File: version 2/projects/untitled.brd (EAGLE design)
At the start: 32.2 x 80.5 mm, 27 parts, among them IC1 LM1117IMPX-3.3, U1 FT232RLSSOP, U2 MCP73831, X2 USB-SMD-NS

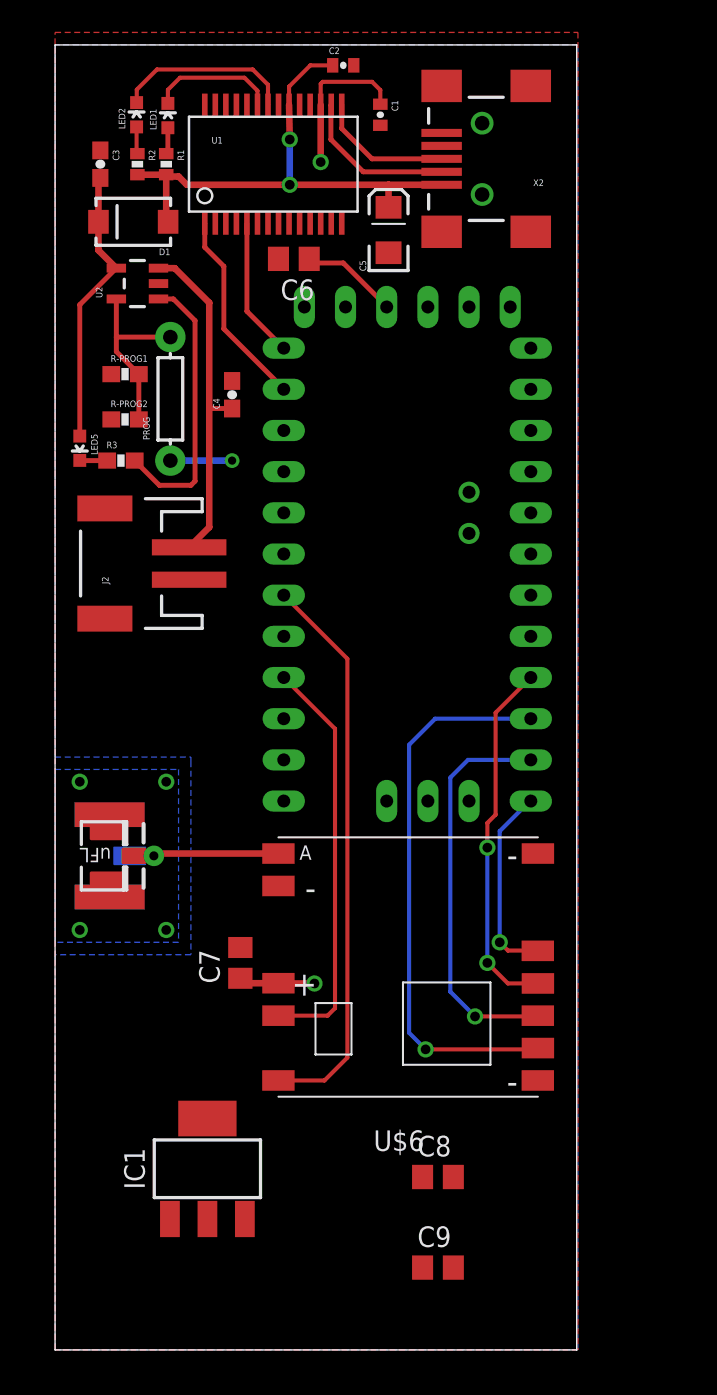
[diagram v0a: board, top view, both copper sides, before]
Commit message: connected \!DTR Pin to RST
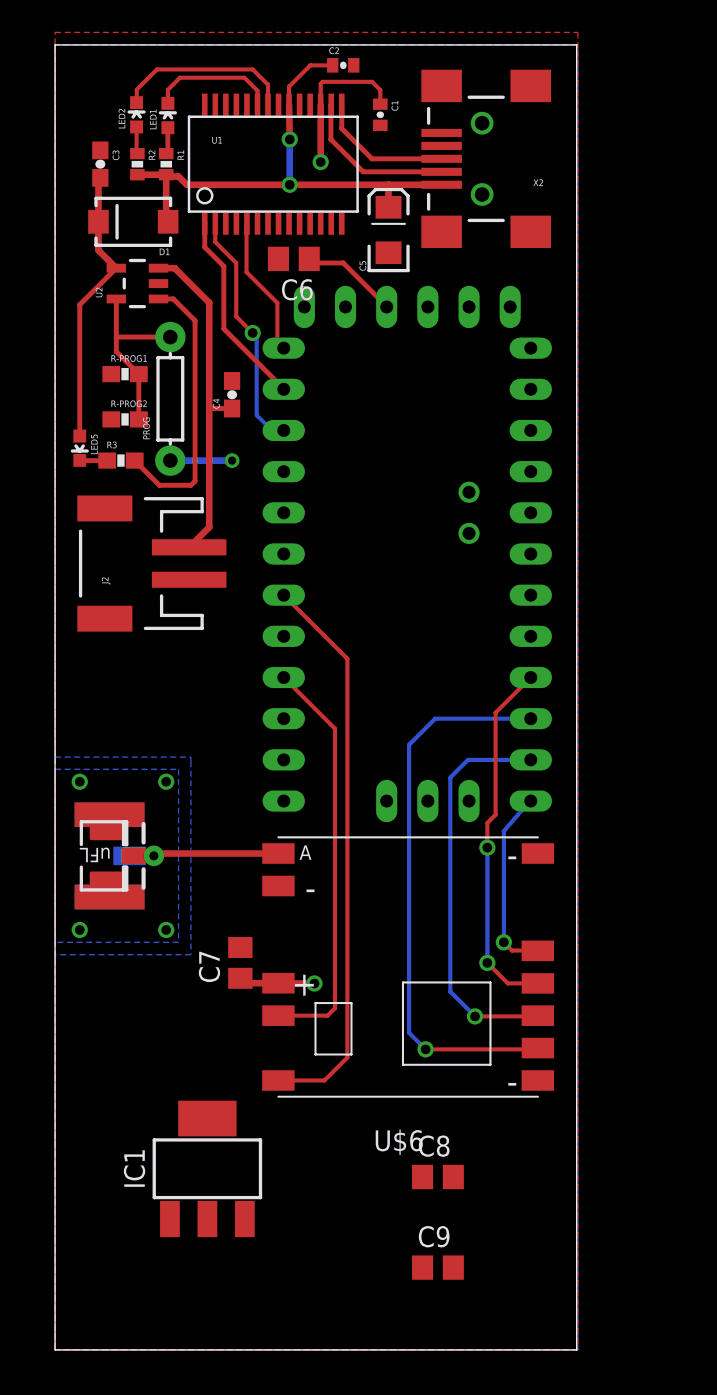
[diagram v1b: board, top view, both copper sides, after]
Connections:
- removed net N$7: U$1.RST1
- net DTR: now also U$1.RST1
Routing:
- net DTR: track 0.00 -> 14.9 mm, vias 0 -> 1
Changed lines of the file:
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@@
 <contactref element="IC1" pad="1"/>
 <wire x1="4.1275" y1="28.448" x2="4.0005" y2="29.51775" width="0" layer="19" extent="1-1"/>
+<wire x1="14.544" y1="67.818" x2="13.899" y2="70.004" width="0" layer="19" extent="1-1"/>
 <wire x1="16.499" y1="77.316" x2="19.192" y2="79.756" width="0" layer="19" extent="1-1"/>
 <wire x1="14.549" y1="77.316" x2="16.499" y2="77.316" width="0" layer="19" extent="1-1"/>
-</signal>
-<signal name="N$7">
-<contactref element="U$1" pad="RST1"/>
 </signal>
 <signal name="N$9">
@@
 <signal name="DTR">
 <contactref element="U1" pad="2"/>
+<contactref element="U$1" pad="RST1"/>
+<wire x1="10.649" y1="68.853" x2="10.649" y2="70.004" width="0.254" layer="1"/>
+<wire x1="11.938" y1="64.262" x2="12.954" y2="63.246" width="0.254" layer="1"/>
+<via x="12.954" y="63.246" extent="1-16" drill="0.6"/>
+<wire x1="11.938" y1="67.564" x2="10.649" y2="68.853" width="0.254" layer="1"/>
+<wire x1="11.938" y1="67.564" x2="11.938" y2="64.262" width="0.254" layer="1"/>
+<wire x1="12.954" y1="63.246" x2="13.208" y2="62.992" width="0.254" layer="16"/>
+<wire x1="13.208" y1="62.992" x2="13.208" y2="58.166" width="0.254" layer="16"/>
+<wire x1="13.208" y1="58.166" x2="14.14409375" y2="57.22990625" width="0.254" layer="16"/>
+<wire x1="14.14409375" y1="57.22990625" x2="14.8714625" y2="57.22990625" width="0.254" layer="16"/>
 </signal>
 <signal name="3.3V" class="1">
@@
 <contactref element="U1" pad="5"/>
 <contactref element="U$1" pad="TX0"/>
-<wire x1="12.599" y1="70.004" x2="12.599" y2="64.58236875" width="0.3048" layer="1"/>
-<wire x1="12.599" y1="64.58236875" x2="14.8714625" y2="62.30990625" width="0.3048" layer="1"/>
+<wire x1="14.8714625" y1="62.30990625" x2="14.478" y2="62.30990625" width="0.254" layer="1"/>
+<wire x1="14.478" y1="65.096628125" x2="12.574171875" y2="67.00045625" width="0.254" layer="1"/>
+<wire x1="12.574171875" y1="67.00045625" x2="12.574171875" y2="69.979171875" width="0.254" layer="1"/>
+<wire x1="12.574171875" y1="69.979171875" x2="12.599" y2="70.004" width="0.254" layer="1"/>
+<wire x1="14.478" y1="62.30990625" x2="14.478" y2="65.096628125" width="0.254" layer="1"/>
 </signal>
 <signal name="POWER">
@@
 <contactref element="U$6" pad="NSS"/>
 <wire x1="30.1114625" y1="34.36990625" x2="30.05190625" y2="34.36990625" width="0.254" layer="1"/>
-<wire x1="28.194" y1="25.654" x2="28.702" y2="25.146" width="0.254" layer="1"/>
-<wire x1="28.702" y1="25.146" x2="30.5265" y2="25.146" width="0.254" layer="1"/>
-<wire x1="30.5265" y1="25.146" x2="30.5425" y2="25.13" width="0.254" layer="1"/>
+<wire x1="30.5425" y1="25.13" x2="30.5265" y2="25.146" width="0.254" layer="1"/>
 <wire x1="30.1114625" y1="34.36990625" x2="30.05190625" y2="34.36990625" width="0.254" layer="16"/>
-<wire x1="30.05190625" y1="34.36990625" x2="28.194" y2="32.512" width="0.254" layer="16"/>
-<wire x1="28.194" y1="32.512" x2="28.194" y2="25.654" width="0.254" layer="16"/>
-<via x="28.194" y="25.654" extent="1-16" drill="0.6"/>
+<wire x1="30.05190625" y1="34.36990625" x2="28.448" y2="32.512" width="0.254" layer="16"/>
+<wire x1="28.448" y1="32.512" x2="28.448" y2="25.654" width="0.254" layer="16"/>
+<via x="28.448" y="25.654" extent="1-16" drill="0.6"/>
+<wire x1="30.5265" y1="25.146" x2="28.956" y2="25.146" width="0.254" layer="1"/>
+<wire x1="28.956" y1="25.146" x2="28.448" y2="25.654" width="0.254" layer="1"/>
 </signal>
 <signal name="N$3">

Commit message: reworked layout. Added voltage controller and discharging mechanism
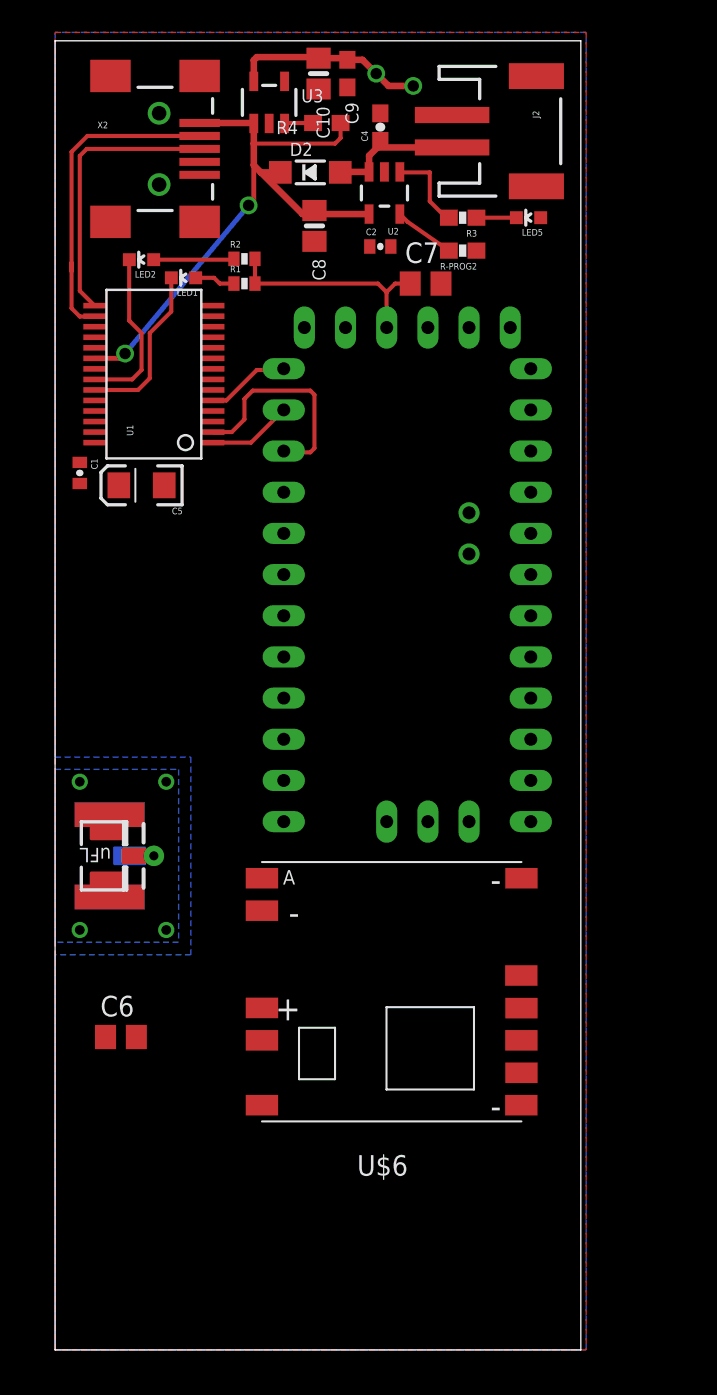
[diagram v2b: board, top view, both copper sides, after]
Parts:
- removed C3: 4.7uF, SparkFun-Capacitors:0603-CAP
- removed D1: MBRA140, SparkFun-DiscreteSemi:SMA-DIODE
- removed IC1: LM1117IMPX-3.3, lm1117:SOT223
- removed PROG: (no value), SparkFun-Resistors:AXIAL-0.3
- removed R-PROG1: 2k, SparkFun-Resistors:0603-RES
- added C10: 10µF, microbuilder:0805-NO
- added D2: MBR120, microbuilder:SOD-123
- added R4: 100k, microbuilder:0603-NO
- added U3: SPX3819-3.3, microbuilder:SOT23-5
- C4: value 4.7uF -> 10u
- C8: value 10u -> 10µF; device rcl:C0805 -> microbuilder:0805-NO
- C9: value 10u -> 1uF; device rcl:C0805 -> microbuilder:0603-NO
- moved C9 73.9 mm to (18.8, 79.2), turned to 270 degrees
- moved C8 59.2 mm to (16.8, 69.8), turned to 270 degrees
- moved C6 49.2 mm to (4.83, 19.8), turned to 0 degrees
- moved C7 43.4 mm to (23.6, 66.3), turned to 0 degrees
- moved J2 35.6 mm to (29.0, 75.7), turned to 270 degrees
- moved LED5 31.1 mm to (30.0, 70.4), turned to 90 degrees
- moved C1 28.8 mm to (2.29, 54.6)
- moved R3 25.9 mm to (25.9, 70.4), turned to 180 degrees
- moved R-PROG2 23.3 mm to (25.9, 68.3), turned to 180 degrees
- moved C5 21.9 mm to (6.10, 53.8), turned to 180 degrees
- moved X2 19.9 mm to (7.18, 74.6), turned to 0 degrees
- moved C4 18.9 mm to (20.8, 75.9)
- moved U2 16.2 mm to (21.1, 71.9), turned to 180 degrees
- moved U1 14.9 mm to (6.86, 60.7), turned to 90 degrees
- moved C2 11.4 mm to (20.8, 68.6)
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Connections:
- removed net N$3: C3.2, D1.C, LED5.A, U2.4
- removed net VCHARGE: C4.1, J2.2, U2.3
- new net +3V3: LED5.A
- new net 123: C1.1, U1.17
- new net EN: R4.2, U3.3
- new net VBAT: C4.1, D2.A, J2.2, U2.3
- net 3.3V: now also C10.1, R1.2, R2.2, U3.5; no longer C1.1, IC1.2, IC1.TAB, U1.17
- net 5V: now also D2.C, R4.1, U2.4, U3.1; no longer D1.A, IC1.3, R1.2, R2.2
- net GND: now also C10.2, U3.2; no longer C3.1, IC1.1, PROG.P$1, R-PROG1.1
- net LOL: no longer PROG.P$2, R-PROG1.2
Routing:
- net D4: track 35.0 -> 0.00 mm
- net MISO: track 34.5 -> 0.00 mm, vias 1 -> 0
- net D6: track 25.4 -> 0.00 mm
- net MOSI: track 24.7 -> 0.00 mm, vias 1 -> 0
- net SCL: track 22.4 -> 0.00 mm, vias 2 -> 0
- net VCHARGE: track 21.1 -> 0.00 mm
- net N$3: track 17.7 -> 0.00 mm
- net N$6: track 17.2 -> 5.24 mm
- net CS: track 11.7 -> 0.00 mm, vias 1 -> 0
- net USB_D-: track 9.81 -> 20.1 mm
- net USB_D+: track 8.39 -> 17.2 mm
- net VBAT: track 0.00 -> 8.60 mm
- net N$4: track 9.26 -> 1.44 mm
- net LOL: track 11.3 -> 3.78 mm
- net TXO: track 12.3 -> 5.19 mm
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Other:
- board size 32.2 x 80.5 mm -> 32.4 x 80.8 mm

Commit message: initial commit
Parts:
- removed J$1: ANTENNATINY, _c2h:SMA_UFL_PAD_TINY
- added J$2: ANTENNATINY, _c2h:SMA_UFL_PAD_TINY
- moved U$6 19.3 mm to (10.7, 39.9), turned to 270 degrees
- moved C6 13.1 mm to (10.7, 31.5), turned to 180 degrees
- moved C7 7.87 mm to (31.5, 66.3)
- moved U$1 6.62 mm to (26.6, 54.2)
- moved LED5 6.60 mm to (36.6, 70.4)
- moved R3 6.35 mm to (32.3, 70.4)
- moved J2 5.84 mm to (34.8, 75.7)
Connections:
- net GND: now also J$2.GND1, J$2.GND2, J$2.GND3, J$2.GND4; no longer J$1.GND1, J$1.GND4
- net N$4: now also J$2.ANT1, J$2.ANT2, J$2.ANT3; no longer J$1.ANT1, J$1.ANT2, J$1.ANT3
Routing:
- net CS: track 0.00 -> 37.2 mm
- net MOSI: track 0.00 -> 32.1 mm
- net SCL: track 0.00 -> 31.1 mm, vias 0 -> 1
- net MISO: track 0.00 -> 28.6 mm
- net N$4: track 1.44 -> 20.5 mm
- net D4: track 0.00 -> 18.7 mm, vias 0 -> 1
- net 3.3V: track 25.7 -> 39.7 mm, vias 2 -> 3
- net D6: track 0.00 -> 11.5 mm, vias 0 -> 1
- net RXI: track 5.17 -> 11.6 mm
- net TXO: track 5.19 -> 11.6 mm
- net N$6: track 5.24 -> 11.6 mm
- net DTR: track 13.5 -> 19.3 mm
- net VBAT: track 8.60 -> 14.4 mm
- net GND: track 0.00 -> 2.24 mm
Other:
- board size 32.4 x 80.8 mm -> 37.8 x 60.4 mm

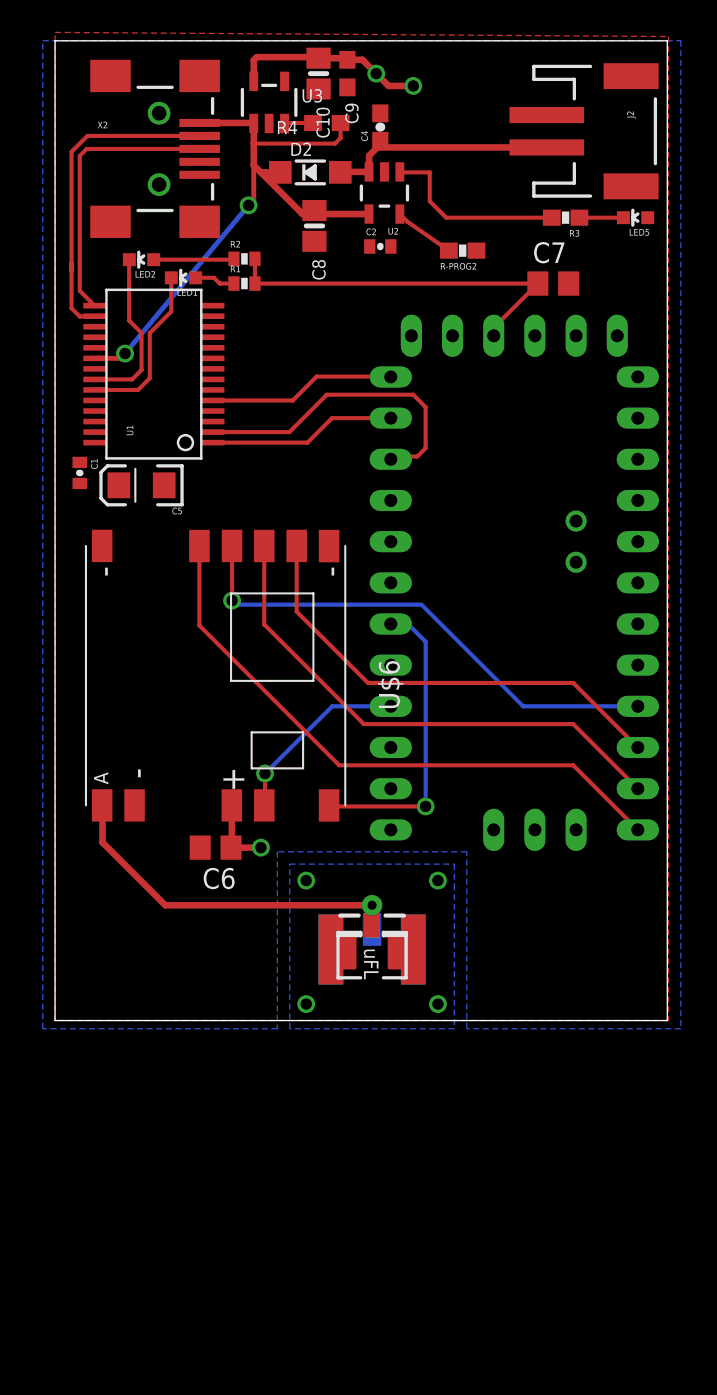
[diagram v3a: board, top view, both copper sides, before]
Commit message: prinzipiell Produktionsreif. Todo: Verkürzen
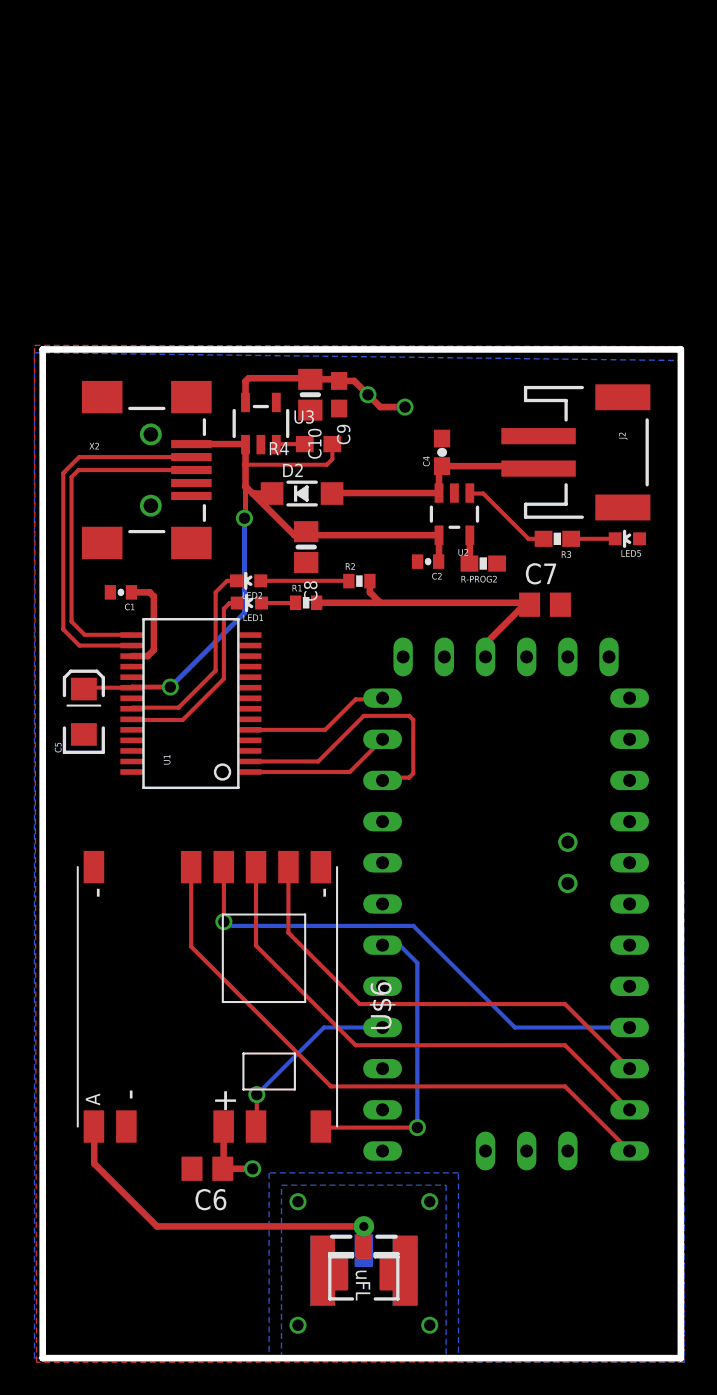
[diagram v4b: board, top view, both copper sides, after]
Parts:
- moved R2 21.1 mm to (19.5, 47.9)
- moved LED2 20.9 mm to (12.7, 48.0)
- moved LED1 20.5 mm to (12.8, 46.6)
- moved U1 20.4 mm to (9.14, 40.4)
- moved C4 20.4 mm to (24.6, 55.9)
- moved U2 20.3 mm to (25.4, 52.1)
- moved R1 20.1 mm to (16.3, 46.6)
- moved C10 19.8 mm to (16.5, 59.4)
- moved C9 19.8 mm to (18.3, 59.4)
- moved LED5 19.8 mm to (36.1, 50.5)
- moved R3 19.8 mm to (31.8, 50.5)
- moved R4 19.8 mm to (17.0, 56.4)
- moved U$6 19.8 mm to (10.2, 20.1)
- moved C6 19.8 mm to (10.2, 11.7)
- moved C7 19.8 mm to (31.0, 46.5)
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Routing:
- net 5V: track 39.0 -> 48.8 mm
- net 123: track 0.00 -> 6.32 mm
- net N$6: track 11.6 -> 5.72 mm
- net 3.3V: track 39.7 -> 36.3 mm
- net USB_D+: track 17.2 -> 20.5 mm
- net N$4: track 20.5 -> 23.3 mm
- net DTR: track 19.3 -> 16.7 mm
- net RXI: track 11.6 -> 8.98 mm
- net TXO: track 11.6 -> 9.00 mm
- net USB_D-: track 20.1 -> 22.6 mm
- net RXLED: track 10.3 -> 12.6 mm
- net LOL: track 3.78 -> 1.76 mm
- net TXLED: track 10.5 -> 12.0 mm
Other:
- board size 37.8 x 60.4 mm -> 39.4 x 62.2 mm

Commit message: Technische Arbeiten abgeschlossen. Logo fehlt noch
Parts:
- moved J$2 17.2 mm to (4.06, 9.91)
- moved C6 6.14 mm to (15.5, 14.7), turned to 0 degrees
- moved U$6 3.34 mm to (9.65, 23.4)
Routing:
- net N$4: track 23.3 -> 5.92 mm
- net 3.3V: track 36.3 -> 46.5 mm
- net D4: track 18.7 -> 10.0 mm
- net SCL: track 31.1 -> 33.3 mm
- net MISO: track 28.6 -> 30.5 mm
- net MOSI: track 32.1 -> 33.8 mm
- net CS: track 37.2 -> 38.3 mm
- net GND: vias 4 -> 0
- removed copper zone on layer 16, net GND
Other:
- board size 39.4 x 62.2 mm -> 39.4 x 53.1 mm
